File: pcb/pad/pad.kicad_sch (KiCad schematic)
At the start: 70 parts, among them J1 781710004, J3 AVR-ISP-6, SW1 SW_Reset, U1 ATmega32U4-A, Y1 16mHz

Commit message: Update pcbs
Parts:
- J1: symbol pico-ezmate:781710004 -> Connector_Generic_MountingPin:Conn_01x04_MountingPin
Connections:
- net GND: now also J1.MP (MountPin)
- net BRow0: now reaches U1.19 (PD1)
- net BCol2: now reaches U1.39 (PF4)
- net BCol1: now reaches U1.40 (PF1)
- net BCol0: now reaches U1.41 (PF0)
- no-connect marks 11 -> 7
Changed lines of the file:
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@@
 	)
 	(no_connect
-		(at 295.91 132.08)
-	)
-	(no_connect
 		(at 265.43 83.82)
 	)
@@
 	)
 	(no_connect
-		(at 295.91 129.54)
-	)
-	(no_connect
 		(at 295.91 121.92)
 	)
@@
 	)
 	(no_connect
-		(at 295.91 93.98)
-	)
-	(no_connect
 		(at 265.43 88.9)
 	)
@@
 	)
 	(no_connect
-		(at 295.91 134.62)
-	)
-	(no_connect
 		(at 295.91 142.24)
 	)
@@
 		)
 	)
+	(global_label "BRow0"
+		(shape input)
+		(at 295.91 101.6 0)
+		(fields_autoplaced yes)
+		(effects
+			(font
+				(size 0.762 0.762)
+			)
+			(justify left)
+		)
+		(property "Intersheetrefs" "${INTERSHEET_REFS}"
+			(at 301.4388 101.6 0)
+			(effects
+				(font
+					(size 1.27 1.27)
+				)
+				(justify left)
+				(hide yes)
+			)
+		)
+	)
 	(global_label "Row1"
 		(shape input)
@@
 		)
 	)
+	(global_label "BCol0"
+		(shape output)
+		(at 295.91 129.54 0)
+		(fields_autoplaced yes)
+		(effects
+			(font
+				(size 0.762 0.762)
+			)
+			(justify left)
+		)
+		(property "Intersheetrefs" "${INTERSHEET_REFS}"
+			(at 304.4589 129.54 0)
+			(effects
+				(font
+					(size 1.27 1.27)
+				)
+				(justify left)
+				(hide yes)
+			)
+		)
+	)
 	(global_label "Col2"
 		(shape output)
@@
 		)
 	)
+	(global_label "BCol2"
+		(shape output)
+		(at 295.91 134.62 0)
+		(fields_autoplaced yes)
+		(effects
+			(font
+				(size 0.762 0.762)
+			)
+			(justify left)
+		)
+		(property "Intersheetrefs" "${INTERSHEET_REFS}"
+			(at 304.4589 134.62 0)
+			(effects
+				(font
+					(size 1.27 1.27)
+				)
+				(justify left)
+				(hide yes)
+			)
+		)
+	)
 	(global_label "Row2"
 		(shape output)
@@
 		)
 	)
+	(global_label "BCol1"
+		(shape output)
+		(at 295.91 132.08 0)
+		(fields_autoplaced yes)
+		(effects
+			(font
+				(size 0.762 0.762)
+			)
+			(justify left)
+		)
+		(property "Intersheetrefs" "${INTERSHEET_REFS}"
+			(at 304.4589 132.08 0)
+			(effects
+				(font
+					(size 1.27 1.27)
+				)
+				(justify left)
+				(hide yes)
+			)
+		)
+	)
 	(global_label "Row4"
 		(shape input)
@@
 	)
 	(symbol
-		(lib_id "pico-ezmate:781710004")
-		(at 353.06 53.34 0)
+		(lib_id "Connector_Generic_MountingPin:Conn_01x04_MountingPin")
+		(at 358.14 55.88 0)
 		(unit 1)
 		(exclude_from_sim no)
@@
 		(fields_autoplaced yes)
 		(property "Reference" "J1"
-			(at 367.03 55.8799 0)
+			(at 360.68 56.2355 0)
 			(effects
 				(font
@@
 		)
 		(property "Value" "781710004"
-			(at 367.03 58.4199 0)
+			(at 360.68 58.7755 0)
 			(effects
 				(font
@@
 		)
 		(property "Footprint" "Connector_Molex:Molex_Pico-EZmate_78171-0004_1x04-1MP_P1.20mm_Vertical"
-			(at 353.06 53.34 0)
+			(at 358.14 55.88 0)
 			(effects
 				(font
 					(size 1.27 1.27)
-					(italic yes)
 				)
 				(hide yes)
 			)
 		)
-		(property "Datasheet" "781710004"
-			(at 353.06 53.34 0)
+		(property "Datasheet" "~"
+			(at 358.14 55.88 0)
 			(effects
 				(font
 					(size 1.27 1.27)
-					(italic yes)
 				)
 				(hide yes)
 			)
 		)
-		(property "Description" ""
-			(at 353.06 53.34 0)
+		(property "Description" "Generic connectable mounting pin connector, single row, 01x04, script generated (kicad-library-utils/schlib/autogen/connector/)"
+			(at 358.14 55.88 0)
 			(effects
 				(font
@@
 		(pin "1"
 		)
+		(pin "MP"
+		)
 		(instances
 			(project ""
@@
 					(unit 1)
 				)
+			)
+		)
+	)
+	(symbol
+		(lib_id "power:GND")
+		(at 358.14 66.04 0)
+		(unit 1)
+		(exclude_from_sim no)
+		(in_bom yes)
+		(on_board yes)
+		(dnp no)
+		(fields_autoplaced yes)
+		(property "Reference" "#PWR014"
+			(at 358.14 72.39 0)
+			(effects
+				(font
+					(size 1.27 1.27)
+				)
+				(hide yes)
+			)
+		)
+		(property "Value" "GND"
+			(at 358.14 71.12 0)
+			(effects
+				(font
+					(size 1.27 1.27)
+				)
+			)
+		)
+		(property "Footprint" ""
+			(at 358.14 66.04 0)
+			(effects
+				(font
+					(size 1.27 1.27)
+				)
+				(hide yes)
+			)
+		)
+		(property "Datasheet" ""
+			(at 358.14 66.04 0)
+			(effects
+				(font
+					(size 1.27 1.27)
+				)
+				(hide yes)
+			)
+		)
+		(property "Description" "Power symbol creates a global label with name \"GND\" , ground"
+			(at 358.14 66.04 0)
+			(effects
+				(font
+					(size 1.27 1.27)
+				)
+				(hide yes)
+			)
+		)
+		(pin "1"
+		)
+		(instances
+			(project "pad"
+				(path "/affa950b-38da-49a2-bb87-68d2039f9d19"
+					(reference "#PWR014")
+					(unit 1)
+				)

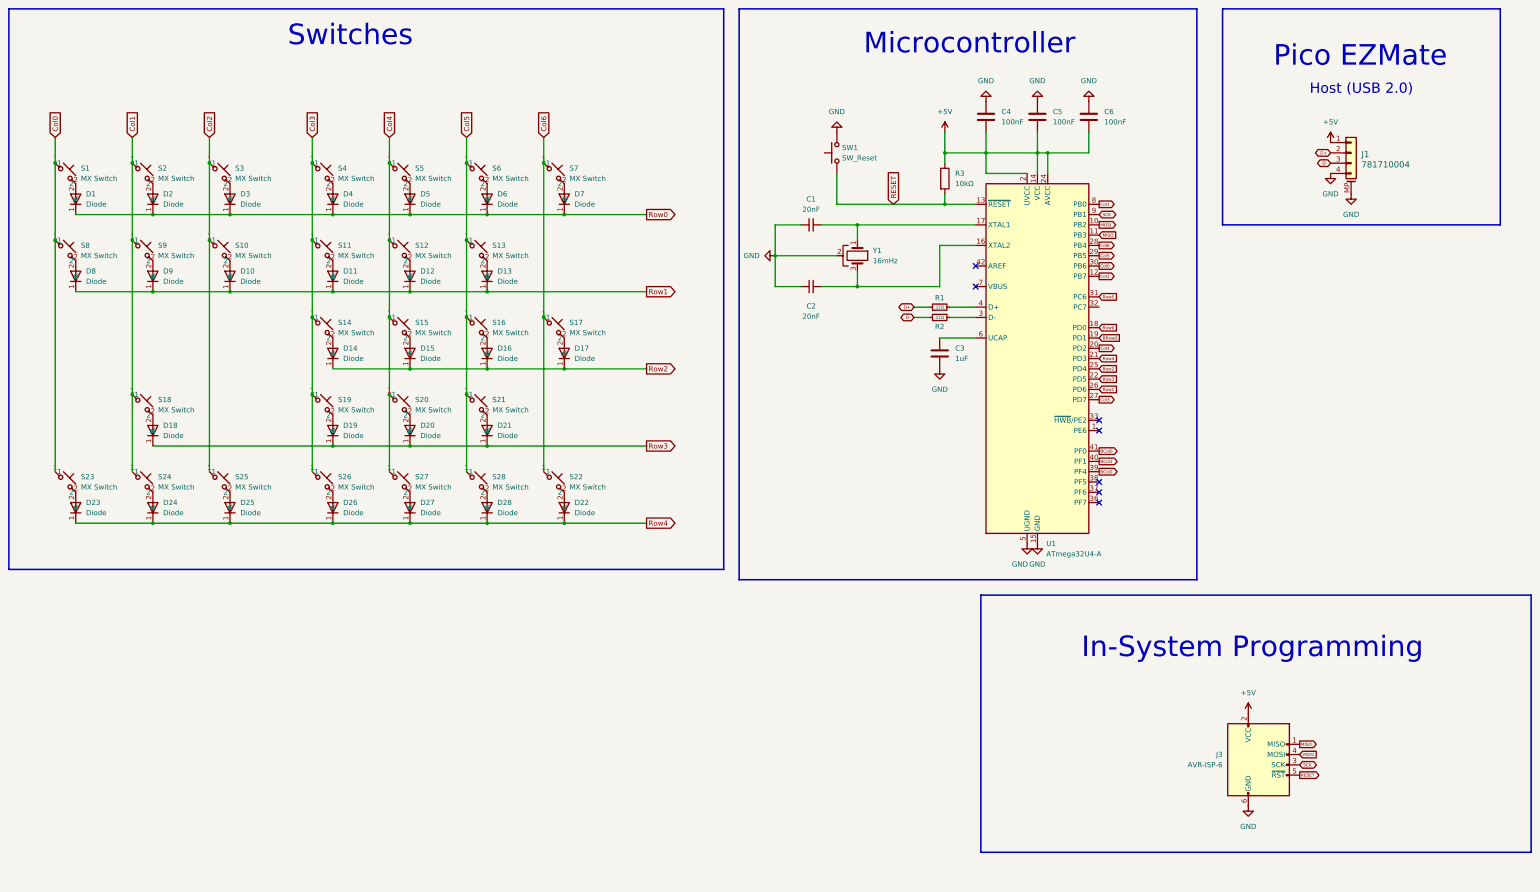
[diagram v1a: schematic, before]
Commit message: Add FPC connector and restart board routing
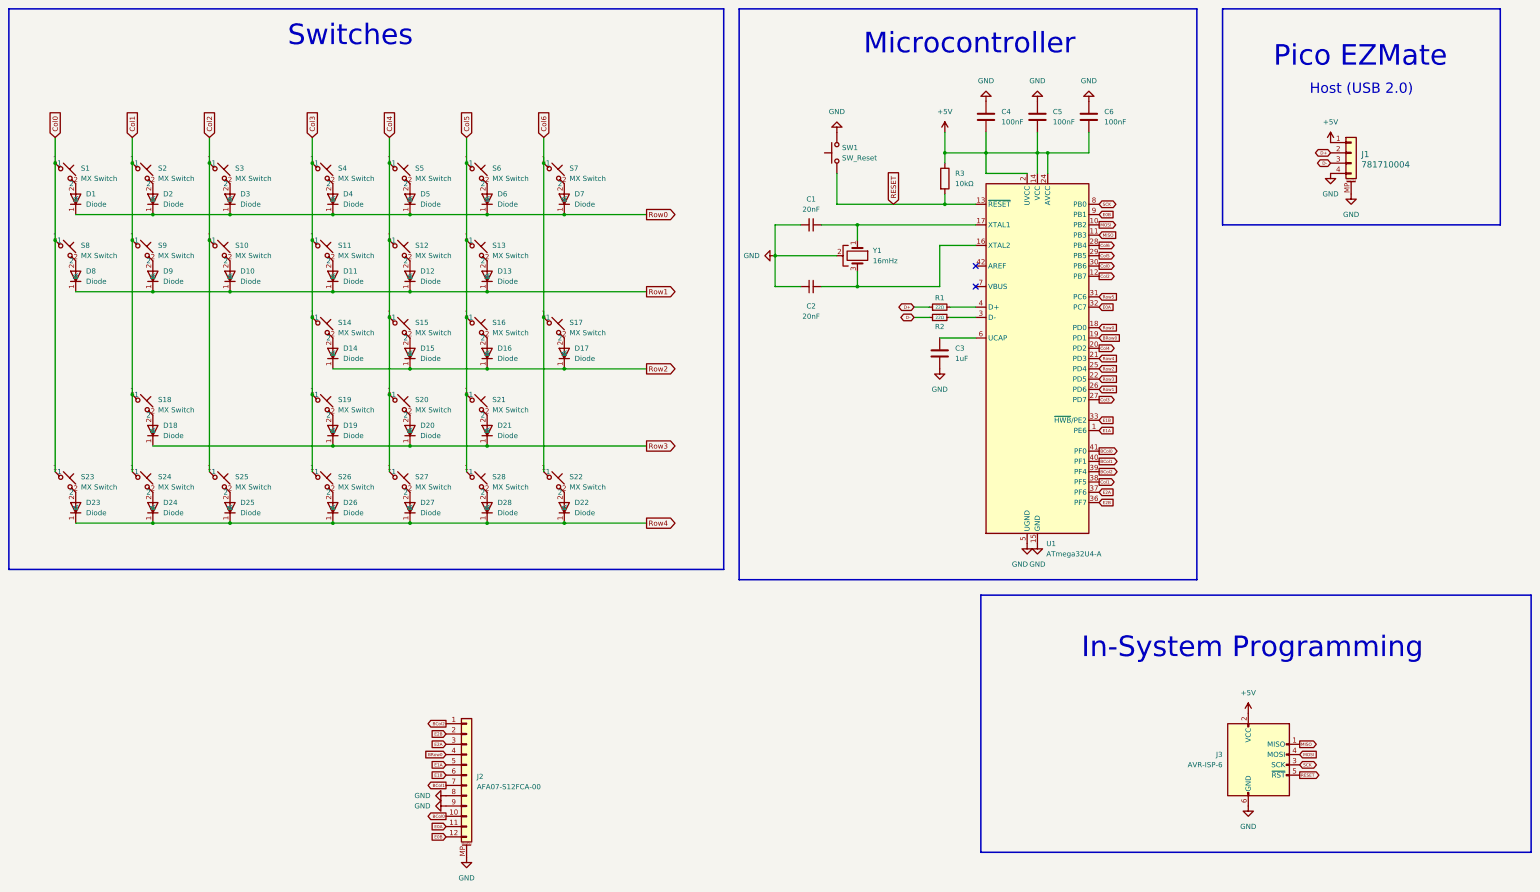
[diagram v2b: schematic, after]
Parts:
- added J2: AFA07-S12FCA-00, Connector_FFC-FPC:JUSHUO_AFA07-S12FCA-00_1x12-1MP_P1.0mm_Horizontal, symbol Connector_Generic_MountingPin:Conn_01x12_MountingPin
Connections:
- net BCol0: now also J2.10 (Pin_10)
- net BCol1: now also J2.7 (Pin_7)
- net BCol2: now also J2.1 (Pin_1)
- net BRow0: now also J2.4 (Pin_4)
- net Col1: now also U1.38 (PF5); no longer U1.8 (PB0)
- net GND: now also J2.8 (Pin_8), J2.9 (Pin_9), J2.MP (MountPin)
- net SCK: now also U1.8 (PB0); no longer U1.9 (PB1)
- net E1A: now reaches U1.1 (PE6)
- net E1A: now also J2.5 (Pin_5)
- net E0A: now reaches U1.32 (PC7)
- net E0A: now also J2.11 (Pin_11)
- net E1B: now reaches U1.33 (~{HWB}/PE2)
- net E1B: now also J2.6 (Pin_6)
- net E2B: now reaches U1.36 (PF7)
- net E2B: now also J2.2 (Pin_2)
- net E2A: now reaches U1.37 (PF6)
- net E2A: now also J2.3 (Pin_3)
- new net E0B: J2.12 (Pin_12), U1.9 (PB1)
- no-connect marks 7 -> 2

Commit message: Update schematic and pcb
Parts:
- J3: now not fitted

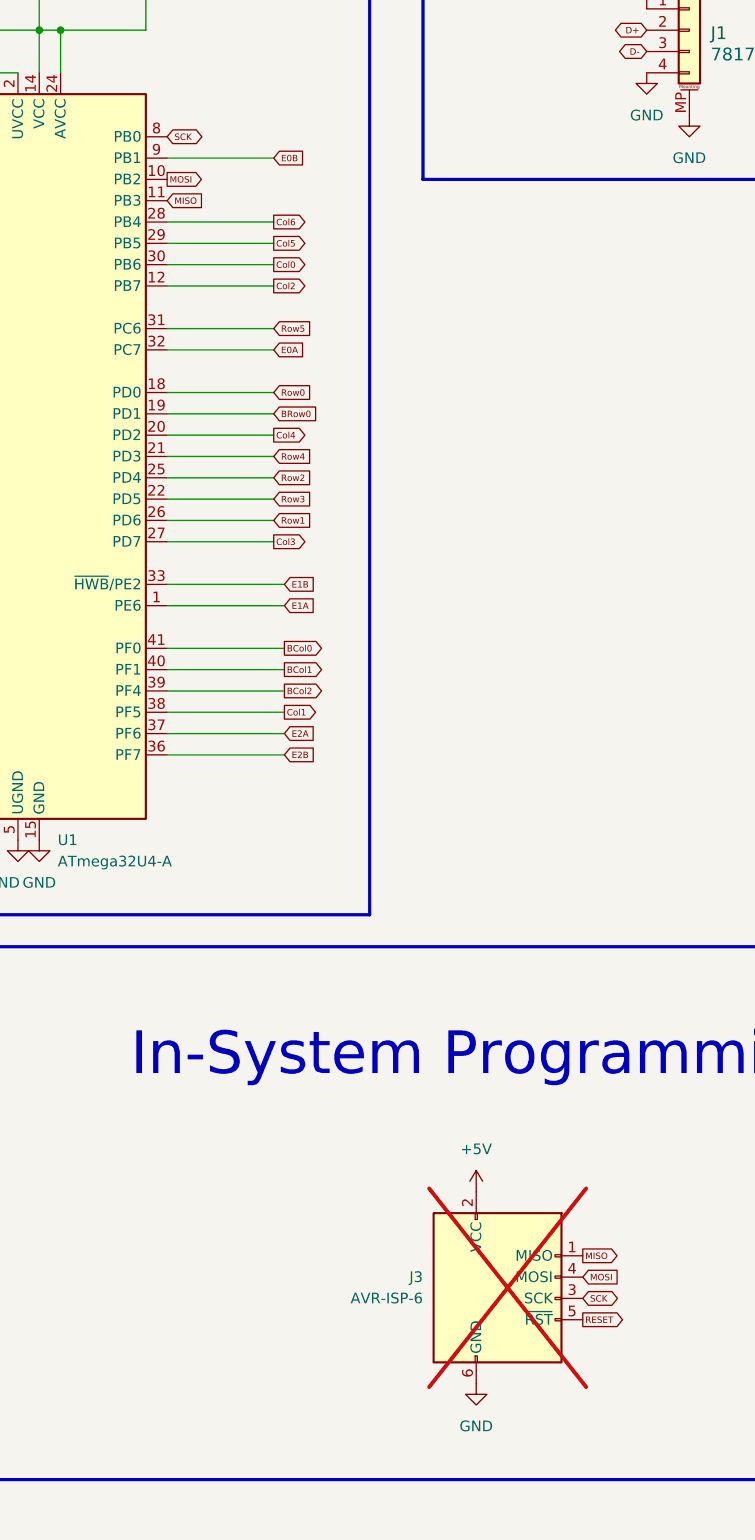
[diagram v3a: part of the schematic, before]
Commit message: Update FPC connectors
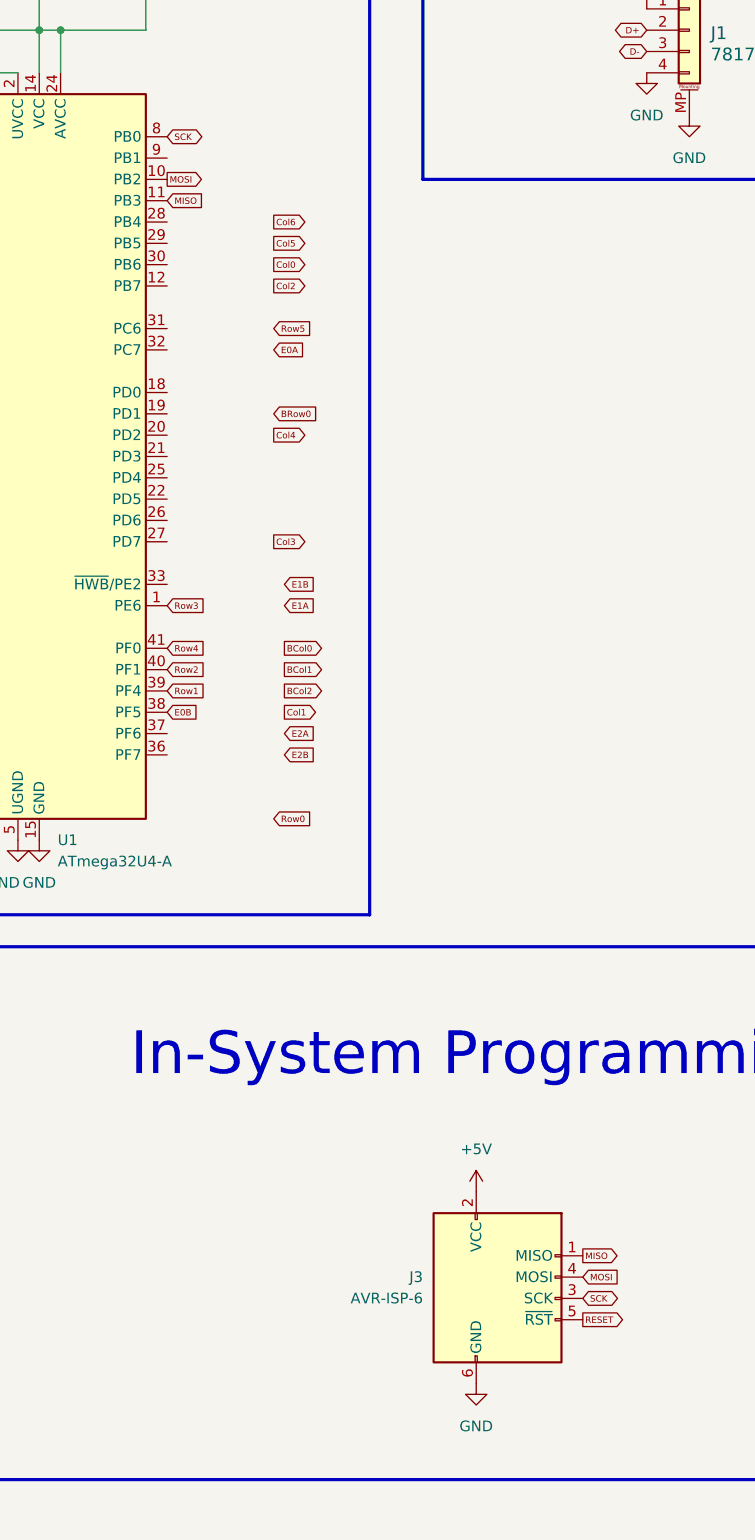
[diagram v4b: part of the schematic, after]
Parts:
- J3: now fitted
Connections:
- net BCol0: no longer U1.41 (PF0)
- net BCol1: no longer U1.40 (PF1)
- net BCol2: no longer U1.39 (PF4)
- net BRow0: no longer U1.19 (PD1)
- net Col0: no longer U1.30 (PB6)
- net Col1: no longer U1.38 (PF5)
- net Col2: no longer U1.12 (PB7)
- net Col3: no longer U1.27 (PD7)
- net Col4: no longer U1.20 (PD2)
- net Col5: no longer U1.29 (PB5)
- net Col6: no longer U1.28 (PB4)
- net E0A: no longer U1.32 (PC7)
- net E0B: now also U1.38 (PF5); no longer U1.9 (PB1)
- net E1A: no longer U1.1 (PE6)
- net E1B: no longer U1.33 (~{HWB}/PE2)
- net E2A: no longer U1.37 (PF6)
- net E2B: no longer U1.36 (PF7)
- net Row0: no longer U1.18 (PD0)
- net Row1: now also U1.39 (PF4); no longer U1.26 (PD6)
- net Row2: now also U1.40 (PF1); no longer U1.25 (PD4)
- net Row3: now also U1.1 (PE6); no longer U1.22 (PD5)
- net Row4: now also U1.41 (PF0); no longer U1.21 (PD3)
- net Row5: no longer U1.31 (PC6)
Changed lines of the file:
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@@
 	(wire
 		(pts
-			(xy 309.88 142.24) (xy 295.91 142.24)
-		)
-		(stroke
-			(width 0)
-			(type default)
-		)
-	)
-	(wire
-		(pts
 			(xy 62.23 128.27) (xy 106.68 128.27)
 		)
@@
 	(wire
 		(pts
-			(xy 308.61 106.68) (xy 295.91 106.68)
-		)
-		(stroke
-			(width 0)
-			(type default)
-		)
-	)
-	(wire
-		(pts
 			(xy 125.73 71.12) (xy 144.78 71.12)
 		)
@@
 	(wire
 		(pts
-			(xy 308.61 91.44) (xy 295.91 91.44)
-		)
-		(stroke
-			(width 0)
-			(type default)
-		)
-	)
-	(wire
-		(pts
 			(xy 81.28 71.12) (xy 106.68 71.12)
 		)
@@
 	(wire
 		(pts
-			(xy 309.88 137.16) (xy 295.91 137.16)
-		)
-		(stroke
-			(width 0)
-			(type default)
-		)
-	)
-	(wire
-		(pts
-			(xy 308.61 104.14) (xy 295.91 104.14)
-		)
-		(stroke
-			(width 0)
-			(type default)
-		)
-	)
-	(wire
-		(pts
 			(xy 106.68 90.17) (xy 125.73 90.17)
 		)
@@
 	(wire
 		(pts
-			(xy 308.61 71.12) (xy 295.91 71.12)
-		)
-		(stroke
-			(width 0)
-			(type default)
-		)
-	)
-	(wire
-		(pts
 			(xy 163.83 109.22) (xy 184.15 109.22)
 		)
@@
 	(wire
 		(pts
-			(xy 295.91 83.82) (xy 308.61 83.82)
-		)
-		(stroke
-			(width 0)
-			(type default)
-		)
-	)
-	(wire
-		(pts
 			(xy 38.1 77.47) (xy 38.1 134.62)
 		)
@@
 	(wire
 		(pts
-			(xy 308.61 114.3) (xy 295.91 114.3)
-		)
-		(stroke
-			(width 0)
-			(type default)
-		)
-	)
-	(wire
-		(pts
-			(xy 308.61 93.98) (xy 295.91 93.98)
-		)
-		(stroke
-			(width 0)
-			(type default)
-		)
-	)
-	(wire
-		(pts
 			(xy 57.15 115.57) (xy 57.15 134.62)
 		)
@@
 	(wire
 		(pts
-			(xy 309.88 132.08) (xy 295.91 132.08)
-		)
-		(stroke
-			(width 0)
-			(type default)
-		)
-	)
-	(wire
-		(pts
 			(xy 257.81 66.04) (xy 257.81 68.58)
 		)
@@
 	(wire
 		(pts
-			(xy 295.91 78.74) (xy 308.61 78.74)
-		)
-		(stroke
-			(width 0)
-			(type default)
-		)
-	)
-	(wire
-		(pts
 			(xy 144.78 147.32) (xy 163.83 147.32)
 		)
@@
 	(wire
 		(pts
-			(xy 295.91 86.36) (xy 308.61 86.36)
-		)
-		(stroke
-			(width 0)
-			(type default)
-		)
-	)
-	(wire
-		(pts
 			(xy 120.65 77.47) (xy 120.65 96.52)
 		)
@@
 	(wire
 		(pts
-			(xy 295.91 81.28) (xy 308.61 81.28)
-		)
-		(stroke
-			(width 0)
-			(type default)
-		)
-	)
-	(wire
-		(pts
 			(xy 101.6 115.57) (xy 101.6 134.62)
 		)
@@
 	(wire
 		(pts
-			(xy 309.88 139.7) (xy 295.91 139.7)
-		)
-		(stroke
-			(width 0)
-			(type default)
-		)
-	)
-	(wire
-		(pts
 			(xy 76.2 58.42) (xy 76.2 77.47)
 		)
@@
 	(wire
 		(pts
-			(xy 308.61 101.6) (xy 295.91 101.6)
-		)
-		(stroke
-			(width 0)
-			(type default)
-		)
-	)
-	(wire
-		(pts
 			(xy 101.6 52.07) (xy 101.6 58.42)
 		)
@@
 	(wire
 		(pts
-			(xy 309.88 121.92) (xy 295.91 121.92)
-		)
-		(stroke
-			(width 0)
-			(type default)
-		)
-	)
-	(wire
-		(pts
 			(xy 139.7 58.42) (xy 139.7 77.47)
 		)
@@
 	(wire
 		(pts
-			(xy 309.88 124.46) (xy 295.91 124.46)
-		)
-		(stroke
-			(width 0)
-			(type default)
-		)
-	)
-	(wire
-		(pts
 			(xy 215.9 73.66) (xy 215.9 81.28)
 		)
@@
 	(wire
 		(pts
-			(xy 309.88 134.62) (xy 295.91 134.62)
-		)
-		(stroke
-			(width 0)
-			(type default)
-		)
-	)
-	(wire
-		(pts
 			(xy 257.81 55.88) (xy 257.81 58.42)
 		)
@@
 	(wire
 		(pts
-			(xy 308.61 111.76) (xy 295.91 111.76)
-		)
-		(stroke
-			(width 0)
-			(type default)
-		)
-	)
-	(wire
-		(pts
 			(xy 57.15 52.07) (xy 57.15 58.42)
 		)
@@
 	(wire
 		(pts
-			(xy 308.61 116.84) (xy 295.91 116.84)
-		)
-		(stroke
-			(width 0)
-			(type default)
-		)
-	)
-	(wire
-		(pts
 			(xy 236.22 88.9) (xy 256.54 88.9)
 		)
@@
 	(wire
 		(pts
-			(xy 308.61 99.06) (xy 295.91 99.06)
-		)
-		(stroke
-			(width 0)
-			(type default)
-		)
-	)
-	(wire
-		(pts
 			(xy 106.68 109.22) (xy 125.73 109.22)
 		)
@@
 	(wire
 		(pts
-			(xy 308.61 109.22) (xy 295.91 109.22)
-		)
-		(stroke
-			(width 0)
-			(type default)
-		)
-	)
-	(wire
-		(pts
 			(xy 76.2 52.07) (xy 76.2 58.42)
 		)
@@
 	(wire
 		(pts
-			(xy 309.88 129.54) (xy 295.91 129.54)
-		)
-		(stroke
-			(width 0)
-			(type default)
-		)
-	)
-	(wire
-		(pts
 			(xy 101.6 77.47) (xy 101.6 96.52)
 		)
@@
 	(global_label "Row0"
 		(shape input)
-		(at 308.61 99.06 0)
+		(at 308.61 149.86 0)
 		(fields_autoplaced yes)
 		(effects
@@
 		)
 		(property "Intersheetrefs" "${INTERSHEET_REFS}"
-			(at 316.5542 99.06 0)
+			(at 316.5542 149.86 0)
 			(effects
 				(font
@@
 	(global_label "Row1"
 		(shape input)
-		(at 308.61 114.3 0)
+		(at 295.91 134.62 0)
 		(fields_autoplaced yes)
 		(effects
@@
 		)
 		(property "Intersheetrefs" "${INTERSHEET_REFS}"
-			(at 316.5542 114.3 0)
+			(at 303.8542 134.62 0)
 			(effects
 				(font
@@
 	(global_label "E0B"
 		(shape input)
-		(at 308.61 71.12 0)
+		(at 295.91 137.16 0)
 		(fields_autoplaced yes)
 		(effects
@@
 		)
 		(property "Intersheetrefs" "${INTERSHEET_REFS}"
-			(at 312.5785 71.12 0)
+			(at 299.8785 137.16 0)
 			(effects
 				(font
@@
 	(global_label "Row3"
 		(shape input)
-		(at 308.61 111.76 0)
+		(at 295.91 124.46 0)
 		(fields_autoplaced yes)
 		(effects
@@
 		)
 		(property "Intersheetrefs" "${INTERSHEET_REFS}"
-			(at 316.5542 111.76 0)
+			(at 303.8542 124.46 0)
 			(effects
 				(font
@@
 	(global_label "Row2"
 		(shape input)
-		(at 308.61 109.22 0)
+		(at 295.91 132.08 0)
 		(fields_autoplaced yes)
 		(effects
@@
 		)
 		(property "Intersheetrefs" "${INTERSHEET_REFS}"
-			(at 316.5542 109.22 0)
+			(at 303.8542 132.08 0)
 			(effects
 				(font
@@
 	(global_label "Row4"
 		(shape input)
-		(at 308.61 106.68 0)
+		(at 295.91 129.54 0)
 		(fields_autoplaced yes)
 		(effects
@@
 		)
 		(property "Intersheetrefs" "${INTERSHEET_REFS}"
-			(at 316.5542 106.68 0)
+			(at 303.8542 129.54 0)
 			(effects
 				(font
@@
 		(in_bom yes)
 		(on_board yes)
-		(dnp yes)
+		(dnp no)
 		(fields_autoplaced yes)
 		(property "Reference" "J3"
